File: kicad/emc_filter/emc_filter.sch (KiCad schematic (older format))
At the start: 9 parts

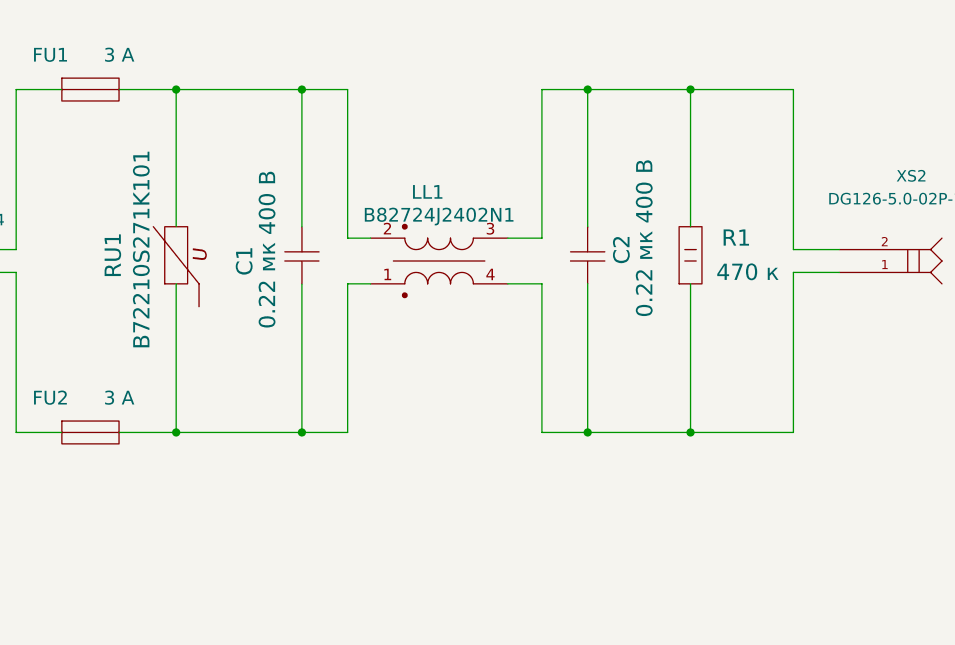
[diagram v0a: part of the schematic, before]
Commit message: Moved to kicad 4.0.0
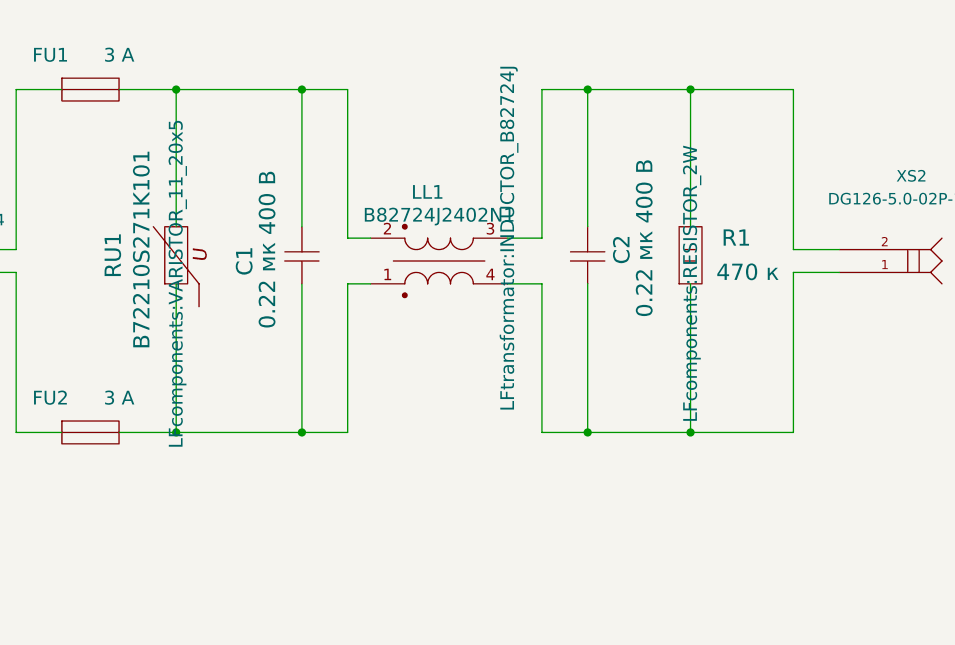
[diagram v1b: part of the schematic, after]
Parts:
- C1, C2: footprint (none) -> LFcomponents:CAPACITOR_15_18x7
- FU1, FU2: footprint (none) -> LFcomponents:FU_PTF15B
- LL1: footprint (none) -> LFtransformator:INDUCTOR_B82724J
- R1: footprint (none) -> LFcomponents:RESISTOR_2W
- RU1: footprint (none) -> LFcomponents:VARISTOR_11_20x5
- XS1, XS2: footprint ~ -> DG126-5.0-02P-14~
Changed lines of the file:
@@
 LIBS:LFtransistor
 LIBS:emc_filter-cache
-EELAYER 27 0
+EELAYER 25 0
 EELAYER END
 $Descr A4 11693 8268
@@
 F 0 "XS2" H 7700 3450 50  0000 L BNN
 F 1 "DG126-5.0-02P-14" H 7400 3550 50  0000 L BNN
-F 2 "~" H 7900 4050 50  0001 C CNN
+F 2 "DG126-5.0-02P-14~" H 7900 4050 50  0001 C CNN
 F 3 "" H 7450 3900 60  0001 C CNN
 	1    7450 3900
@@
 F 0 "FU2" H 4000 4750 60  0000 C CNN
 F 1 "3 A" H 4300 4750 60  0000 C CNN
-F 2 "" H 4050 4600 60  0001 C CNN
+F 2 "LFcomponents:FU_PTF15B" H 4050 4600 60  0001 C CNN
 F 3 "" H 4050 4600 60  0001 C CNN
 	1    4050 4600
@@
 F 0 "FU1" H 4000 3250 60  0000 C CNN
 F 1 "3 A" H 4300 3250 60  0000 C CNN
-F 2 "" H 4050 3100 60  0001 C CNN
+F 2 "LFcomponents:FU_PTF15B" H 4050 3100 60  0001 C CNN
 F 3 "" H 4050 3100 60  0001 C CNN
 	1    4050 3100
@@
 F 0 "XS1" H 3750 4000 50  0000 L BNN
 F 1 "DG126-5.0-02P-14" H 3400 3900 50  0000 L BNN
-F 2 "~" H 4050 3950 50  0001 C CNN
+F 2 "DG126-5.0-02P-14~" H 4050 3950 50  0001 C CNN
 F 3 "" H 3600 3800 60  0001 C CNN
 	1    3600 3800
@@
 F 0 "R1" V 7000 3750 71  0000 C CNN
 F 1 "470 к" V 6850 3700 71  0000 C CNN
-F 2 "" H 6800 3950 60  0000 C CNN
+F 2 "LFcomponents:RESISTOR_2W" H 6800 3950 60  0000 C CNN
 F 3 "" H 6800 3950 60  0000 C CNN
 	1    6800 3950
@@
 	7450 3900 7250 3900
 Wire Wire Line
-	7250 4600 7250 3900
+	7250 3900 7250 4600
 Wire Wire Line
 	6800 3100 6800 3700
@@
 F 0 "C2" H 6500 3800 71  0000 C CNN
 F 1 "0.22 мк 400 В" H 6550 3700 71  0000 C CNN
-F 2 "" H 6350 3950 60  0001 C CNN
+F 2 "LFcomponents:CAPACITOR_15_18x7" H 6350 3950 60  0001 C CNN
 F 3 "" H 6350 3950 60  0001 C CNN
 	1    6350 3950
@@
 F 0 "C1" H 5200 3700 71  0000 C CNN
 F 1 "0.22 мк 400 В" H 5250 3800 71  0000 C CNN
-F 2 "" H 5100 3950 60  0001 C CNN
+F 2 "LFcomponents:CAPACITOR_15_18x7" H 5100 3950 60  0001 C CNN
 F 3 "" H 5100 3950 60  0001 C CNN
 	1    5100 3950
@@
 F 0 "RU1" H 4675 4225 71  0000 C CNN
 F 1 "B72210S271K101" H 4700 4100 71  0000 C CNN
-F 2 "" H 4550 3950 60  0000 C CNN
+F 2 "LFcomponents:VARISTOR_11_20x5" H 4550 3950 60  0000 C CNN
 F 3 "" H 4550 3950 60  0000 C CNN
 	1    4550 3950
@@
 F 0 "LL1" V 5800 3400 60  0000 C CNN
 F 1 "B82724J2402N1" V 5900 3450 60  0000 C CNN
-F 2 "" H 6000 3750 60  0000 C CNN
+F 2 "LFtransformator:INDUCTOR_B82724J" H 6000 3750 60  0000 C CNN
 F 3 "" H 6000 3750 60  0000 C CNN
 	1    6000 3750
